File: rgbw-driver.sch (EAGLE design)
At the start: 16 parts, among them J1 M20, J2 M20, Q1 STN4NF03L, Q2 STN4NF03L, Q3 STN4NF03L, Q4 STN4NF03L, X1 2PIN

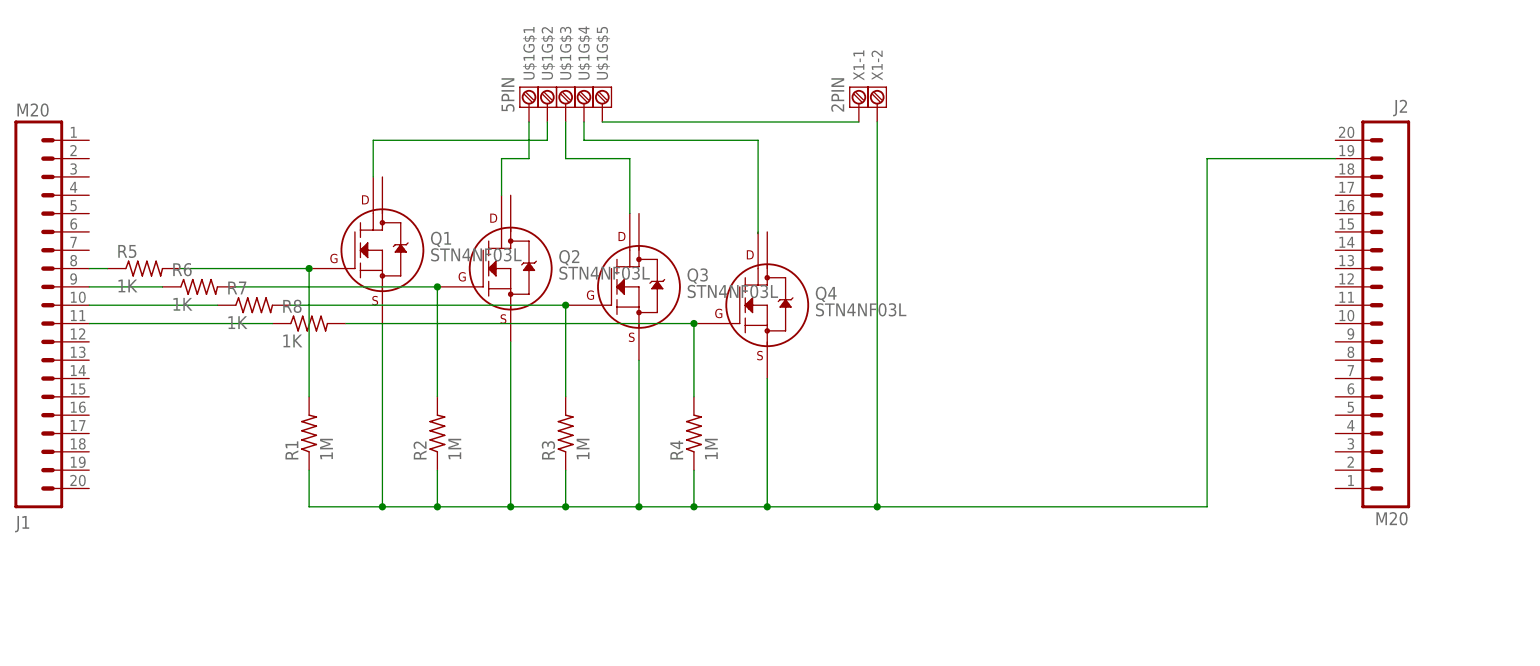
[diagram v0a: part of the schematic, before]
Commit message: Modifications to allow large heatsink for high current usage
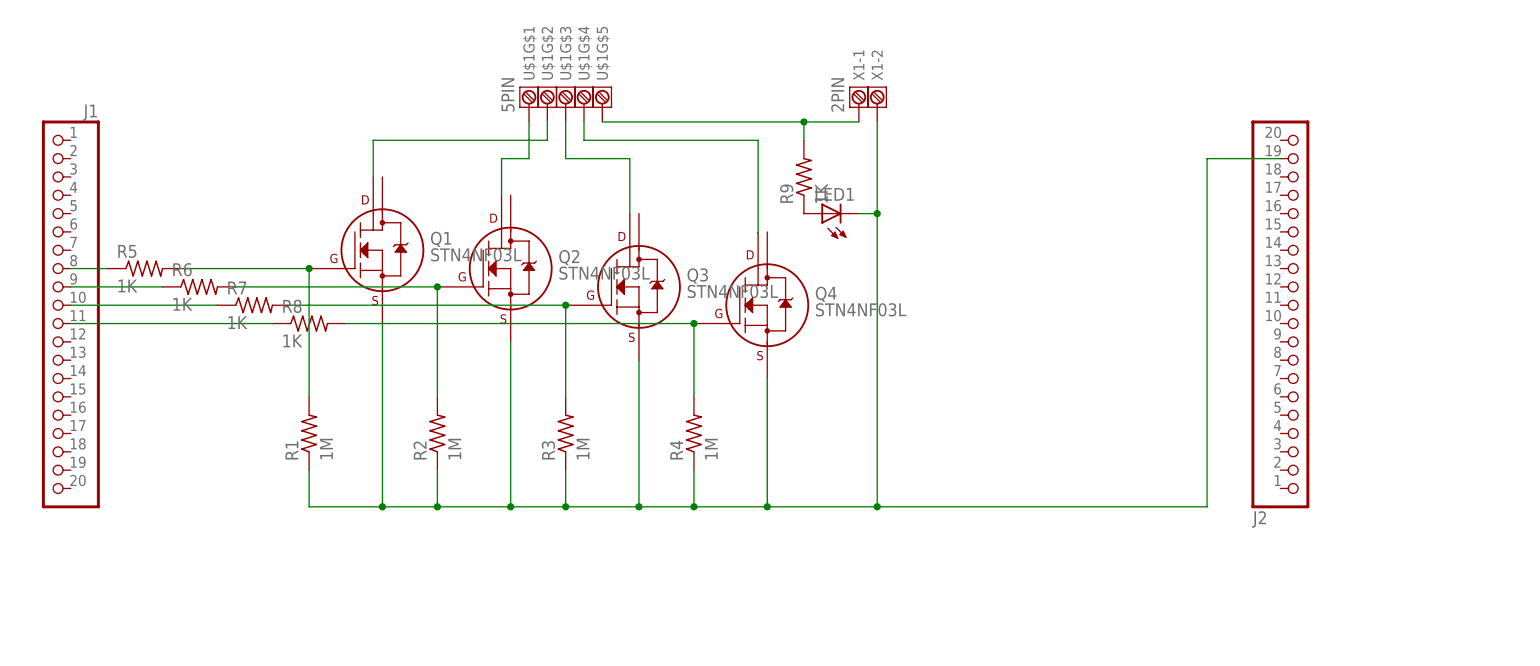
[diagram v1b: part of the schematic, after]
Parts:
- added LED1: (no value), led:LEDCHIP-LED0805
- added R9: 1K, rcl:R-US_R0805
- J1, J2: value M20 -> (none); device SparkFun3:M20 -> header:PINHD-1X20
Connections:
- removed net V+: U$1G$5.1, X1-1.1
- new net N$3: LED1.A, R9.1
- new net N$6: R9.2, U$1G$5.1, X1-1.1
- net N$4: now also LED1.C
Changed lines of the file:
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@@
 <layer number="54" name="bGND_GNDA" color="1" fill="9" visible="no" active="no"/>
 <layer number="56" name="wert" color="7" fill="1" visible="no" active="no"/>
+<layer number="57" name="tCAD" color="7" fill="1" visible="no" active="no"/>
 <layer number="91" name="Nets" color="2" fill="1" visible="yes" active="yes"/>
 <layer number="92" name="Busses" color="1" fill="1" visible="yes" active="yes"/>
@@
 <layer number="97" name="Info" color="7" fill="1" visible="yes" active="yes"/>
 <layer number="98" name="Guide" color="6" fill="1" visible="yes" active="yes"/>
+<layer number="99" name="SpiceOrder" color="7" fill="1" visible="no" active="no"/>
 <layer number="100" name="Muster" color="7" fill="1" visible="no" active="no"/>
 <layer number="101" name="Patch_Top" color="12" fill="4" visible="yes" active="yes"/>
@@
 <layer number="106" name="bPlate" color="7" fill="1" visible="yes" active="yes"/>
 <layer number="107" name="Crop" color="7" fill="1" visible="yes" active="yes"/>
+<layer number="108" name="fp8" color="7" fill="1" visible="no" active="yes"/>
+<layer number="109" name="fp9" color="7" fill="1" visible="no" active="yes"/>
+<layer number="110" name="fp0" color="7" fill="1" visible="no" active="yes"/>
+<layer number="111" name="LPC17xx" color="7" fill="1" visible="no" active="yes"/>
+<layer number="112" name="tSilk" color="7" fill="1" visible="no" active="yes"/>
+<layer number="113" name="ReferenceLS" color="7" fill="1" visible="no" active="no"/>
 <layer number="116" name="Patch_BOT" color="9" fill="4" visible="yes" active="yes"/>
+<layer number="118" name="Rect_Pads" color="7" fill="1" visible="no" active="no"/>
 <layer number="121" name="_tsilk" color="7" fill="1" visible="yes" active="yes"/>
 <layer number="122" name="_bsilk" color="7" fill="1" visible="yes" active="yes"/>
+<layer number="123" name="tTestmark" color="7" fill="1" visible="no" active="yes"/>
+<layer number="124" name="bTestmark" color="7" fill="1" visible="no" active="yes"/>
+<layer number="125" name="_tNames" color="7" fill="1" visible="no" active="yes"/>
+<layer number="126" name="_bNames" color="7" fill="1" visible="no" active="yes"/>
+<layer number="127" name="_tValues" color="7" fill="1" visible="no" active="yes"/>
+<layer number="128" name="_bValues" color="7" fill="1" visible="no" active="yes"/>
+<layer number="131" name="tAdjust" color="7" fill="1" visible="no" active="yes"/>
+<layer number="132" name="bAdjust" color="7" fill="1" visible="no" active="yes"/>
+<layer number="144" name="Drill_legend" color="7" fill="1" visible="no" active="yes"/>
+<layer number="150" name="Notes" color="7" fill="1" visible="no" active="yes"/>
 <layer number="151" name="HeatSink" color="7" fill="1" visible="yes" active="yes"/>
+<layer number="152" name="_bDocu" color="7" fill="1" visible="no" active="yes"/>
+<layer number="153" name="FabDoc1" color="6" fill="1" visible="no" active="no"/>
+<layer number="154" name="FabDoc2" color="2" fill="1" visible="no" active="no"/>
+<layer number="155" name="FabDoc3" color="7" fill="15" visible="no" active="no"/>
 <layer number="199" name="Contour" color="7" fill="1" visible="no" active="yes"/>
 <layer number="200" name="200bmp" color="1" fill="10" visible="yes" active="yes"/>
@@
 <layer number="207" name="207bmp" color="8" fill="10" visible="yes" active="yes"/>
 <layer number="208" name="208bmp" color="9" fill="10" visible="yes" active="yes"/>
+<layer number="209" name="209bmp" color="7" fill="1" visible="no" active="yes"/>
+<layer number="210" name="210bmp" color="7" fill="1" visible="no" active="yes"/>
+<layer number="211" name="211bmp" color="7" fill="1" visible="no" active="yes"/>
+<layer number="212" name="212bmp" color="7" fill="1" visible="no" active="yes"/>
+<layer number="213" name="213bmp" color="7" fill="1" visible="no" active="yes"/>
+<layer number="214" name="214bmp" color="7" fill="1" visible="no" active="yes"/>
+<layer number="215" name="215bmp" color="7" fill="1" visible="no" active="yes"/>
+<layer number="216" name="216bmp" color="7" fill="1" visible="no" active="yes"/>
+<layer number="217" name="217bmp" color="18" fill="1" visible="no" active="no"/>
+<layer number="218" name="218bmp" color="19" fill="1" visible="no" active="no"/>
+<layer number="219" name="219bmp" color="20" fill="1" visible="no" active="no"/>
+<layer number="220" name="220bmp" color="21" fill="1" visible="no" active="no"/>
+<layer number="221" name="221bmp" color="22" fill="1" visible="no" active="no"/>
+<layer number="222" name="222bmp" color="23" fill="1" visible="no" active="no"/>
+<layer number="223" name="223bmp" color="24" fill="1" visible="no" active="no"/>
+<layer number="224" name="224bmp" color="25" fill="1" visible="no" active="no"/>
+<layer number="231" name="Eagle3D_PG1" color="7" fill="1" visible="no" active="no"/>
+<layer number="232" name="Eagle3D_PG2" color="7" fill="1" visible="no" active="no"/>
+<layer number="233" name="Eagle3D_PG3" color="7" fill="1" visible="no" active="no"/>
+<layer number="248" name="Housing" color="7" fill="1" visible="no" active="yes"/>
+<layer number="249" name="Edge" color="7" fill="1" visible="no" active="yes"/>
 <layer number="250" name="Descript" color="3" fill="1" visible="no" active="no"/>
 <layer number="251" name="SMDround" color="12" fill="11" visible="no" active="no"/>
@@
 </classes>
 <parts>
-<part name="J1" library="SparkFun3" deviceset="M20" device=""/>
-<part name="J2" library="SparkFun3" deviceset="M20" device=""/>
+<part name="J1" library="header" deviceset="PINHD-1X20" device=""/>
+<part name="J2" library="header" deviceset="PINHD-1X20" device=""/>
 <part name="FRAME1" library="SparkFun3" deviceset="FRAME-A3" device=""/>
 <part name="R5" library="resistor" deviceset="R-US_" device="R0805" value="1K"/>
@@
 <part name="U$1" library="con-3.81" deviceset="5PIN" device=""/>
 <part name="X1" library="con-3.81" deviceset="2PIN" device=""/>
+<part name="LED1" library="led" deviceset="LED" device="CHIP-LED0805"/>
+<part name="R9" library="rcl" deviceset="R-US_" device="R0805" value="1K"/>
 </parts>
 <sheets>
@@
 </plain>
 <instances>
-<instance part="J1" gate="G$1" x="116.84" y="198.12" rot="MR180"/>
-<instance part="J2" gate="G$1" x="309.88" y="139.7" rot="MR0"/>
+<instance part="J1" gate="A" x="121.92" y="170.18" rot="MR0"/>
+<instance part="J2" gate="A" x="294.64" y="167.64" rot="MR180"/>
 <instance part="FRAME1" gate="G$1" x="0" y="0"/>
 <instance part="R5" gate="G$1" x="134.62" y="175.26"/>
@@
 <instance part="X1" gate="-1" x="233.68" y="198.12" rot="MR270"/>
 <instance part="X1" gate="-2" x="236.22" y="198.12" rot="MR270"/>
+<instance part="LED1" gate="G$1" x="228.6" y="182.88" rot="R90"/>
+<instance part="R9" gate="G$1" x="226.06" y="187.96" rot="R90"/>
 </instances>
 <busses>
@@
 <net name="N$1" class="0">
 <segment>
-<pinref part="J1" gate="G$1" pin="8"/>
+<pinref part="J1" gate="A" pin="8"/>
 <pinref part="R5" gate="G$1" pin="1"/>
-<wire x1="127" y1="175.26" x2="129.54" y2="175.26" width="0.1524" layer="91"/>
+<wire x1="124.46" y1="175.26" x2="129.54" y2="175.26" width="0.1524" layer="91"/>
 </segment>
 </net>
@@
 <segment>
 <wire x1="281.94" y1="142.24" x2="281.94" y2="190.5" width="0.1524" layer="91"/>
-<pinref part="J2" gate="G$1" pin="19"/>
-<wire x1="281.94" y1="190.5" x2="299.72" y2="190.5" width="0.1524" layer="91"/>
+<pinref part="J2" gate="A" pin="19"/>
+<wire x1="281.94" y1="190.5" x2="292.1" y2="190.5" width="0.1524" layer="91"/>
 <wire x1="157.48" y1="142.24" x2="167.64" y2="142.24" width="0.1524" layer="91"/>
 <pinref part="R1" gate="G$1" pin="1"/>
@@
 <junction x="220.98" y="142.24"/>
 <pinref part="X1" gate="-2" pin="1"/>
-<wire x1="236.22" y1="195.58" x2="236.22" y2="142.24" width="0.1524" layer="91"/>
 <junction x="236.22" y="142.24"/>
+<wire x1="236.22" y1="195.58" x2="236.22" y2="182.88" width="0.1524" layer="91"/>
+<pinref part="LED1" gate="G$1" pin="C"/>
+<wire x1="236.22" y1="182.88" x2="236.22" y2="142.24" width="0.1524" layer="91"/>
+<wire x1="233.68" y1="182.88" x2="236.22" y2="182.88" width="0.1524" layer="91"/>
+<junction x="236.22" y="182.88"/>
 </segment>
 </net>
 <net name="N$8" class="0">
 <segment>
-<pinref part="J1" gate="G$1" pin="9"/>
+<pinref part="J1" gate="A" pin="9"/>
 <pinref part="R6" gate="G$1" pin="1"/>
-<wire x1="127" y1="172.72" x2="137.16" y2="172.72" width="0.1524" layer="91"/>
+<wire x1="124.46" y1="172.72" x2="137.16" y2="172.72" width="0.1524" layer="91"/>
 </segment>
 </net>
 <net name="N$9" class="0">
 <segment>
-<pinref part="J1" gate="G$1" pin="10"/>
+<pinref part="J1" gate="A" pin="10"/>
 <pinref part="R7" gate="G$1" pin="1"/>
-<wire x1="127" y1="170.18" x2="144.78" y2="170.18" width="0.1524" layer="91"/>
+<wire x1="124.46" y1="170.18" x2="144.78" y2="170.18" width="0.1524" layer="91"/>
 </segment>
 </net>
 <net name="N$10" class="0">
 <segment>
-<pinref part="J1" gate="G$1" pin="11"/>
+<pinref part="J1" gate="A" pin="11"/>
 <pinref part="R8" gate="G$1" pin="1"/>
-<wire x1="127" y1="167.64" x2="152.4" y2="167.64" width="0.1524" layer="91"/>
+<wire x1="124.46" y1="167.64" x2="152.4" y2="167.64" width="0.1524" layer="91"/>
 </segment>
 </net>
@@
 </segment>
 </net>
-<net name="V+" class="0">
+<net name="N$6" class="0">
 <segment>
 <pinref part="U$1" gate="G$5" pin="1"/>
 <pinref part="X1" gate="-1" pin="1"/>
-<wire x1="198.12" y1="195.58" x2="233.68" y2="195.58" width="0.1524" layer="91"/>
-</segment>
-</net>
+<wire x1="198.12" y1="195.58" x2="226.06" y2="195.58" width="0.1524" layer="91"/>
+<pinref part="R9" gate="G$1" pin="2"/>
+<wire x1="226.06" y1="195.58" x2="233.68" y2="195.58" width="0.1524" layer="91"/>
+<wire x1="226.06" y1="195.58" x2="226.06" y2="193.04" width="0.1524" layer="91"/>
+<junction x="226.06" y="195.58"/>
+</segment>
+</net>
+<net name="N$3" class="0">
+<segment>
+<pinref part="R9" gate="G$1" pin="1"/>
+<pinref part="LED1" gate="G$1" pin="A"/>
+</segment>
+</net>
